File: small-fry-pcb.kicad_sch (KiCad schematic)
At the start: 139 parts, among them U1 Pico

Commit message: Squashed commit of the following:
commit e493926800ae8eeeb9c8551a418d401659cc4f4a
Author: anchovie-codes <littlebrother.free@gmail.com>
Date:   Sun Nov 10 19:39:24 2024 -0500

    updated edge cuts and gerbers

commit a852bf54e9e750d94bc40db8a16316f7cdac5ac1
Author: anchovie-codes <littlebrother.free@gmail.com>
Date:   Sat Sep 28 17:49:30 2024 -0400

    fixed rows, generated gerbers

commit 9d77bf2fb49dd0b8cbfb8cfda25d822d23244967
Author: anchovie-codes <littlebrother.free@gmail.com>
Date:   Sat Sep 28 13:01:13 2024 -0400

    fixed cols

commit 5f5487953ddbebd1258b34876b9f208a7da505d8
Author: anchovie-codes <littlebrother.free@gmail.com>
Date:   Fri Sep 27 21:14:36 2024 -0400

    made it a fish
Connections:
- net col0: now also U1.20 (GPIO15); no longer U1.19 (GPIO14)
- net col1: now also U1.19 (GPIO14); no longer U1.17 (GPIO13)
- net col10: now also U1.27 (GPIO21); no longer U1.6 (GPIO4)
- net col11: now also U1.26 (GPIO20); no longer U1.5 (GPIO3)
- net col12: now also U1.25 (GPIO19); no longer U1.4 (GPIO2)
- net col13: now also U1.24 (GPIO18); no longer U1.2 (GPIO1)
- net col14: now also U1.22 (GPIO17); no longer U1.1 (GPIO0)
- net col2: now also U1.17 (GPIO13); no longer U1.16 (GPIO12)
- net col3: now also U1.16 (GPIO12); no longer U1.15 (GPIO11)
- net col4: now also U1.15 (GPIO11); no longer U1.14 (GPIO10)
- net col5: now also U1.14 (GPIO10); no longer U1.12 (GPIO9)
- net col6: now also U1.12 (GPIO9); no longer U1.11 (GPIO8)
- net col7: now also U1.32 (GPIO27_ADC1); no longer U1.10 (GPIO7)
- net col8: now also U1.31 (GPIO26_ADC0); no longer U1.9 (GPIO6)
- net col9: now also U1.29 (GPIO22); no longer U1.7 (GPIO5)
- net row0: now also U1.6 (GPIO4); no longer U1.27 (GPIO21)
- net row1: now also U1.7 (GPIO5); no longer U1.26 (GPIO20)
- net row2: now also U1.9 (GPIO6); no longer U1.25 (GPIO19)
- net row3: now also U1.10 (GPIO7); no longer U1.24 (GPIO18)
- net row4: now also U1.11 (GPIO8); no longer U1.22 (GPIO17)
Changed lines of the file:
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@@
 	)
 	(no_connect
+		(at 20.32 29.21)
+	)
+	(no_connect
 		(at 55.88 69.85)
 	)
@@
 	)
 	(no_connect
-		(at 55.88 41.91)
+		(at 20.32 26.67)
 	)
 	(no_connect
@@
 	)
 	(no_connect
-		(at 55.88 54.61)
+		(at 55.88 41.91)
 	)
 	(no_connect
-		(at 55.88 49.53)
+		(at 40.64 80.01)
 	)
 	(no_connect
-		(at 40.64 80.01)
+		(at 20.32 34.29)
 	)
 	(no_connect
@@
 	)
 	(no_connect
-		(at 20.32 74.93)
-	)
-	(no_connect
-		(at 55.88 46.99)
+		(at 20.32 36.83)
 	)
 	(no_connect
@@
 		)
 	)
-	(global_label "col14"
-		(shape input)
-		(at 20.32 26.67 180)
-		(fields_autoplaced yes)
-		(effects
-			(font
-				(size 1.27 1.27)
-			)
-			(justify right)
-		)
-		(property "Intersheetrefs" "${INTERSHEET_REFS}"
-			(at 12.6672 26.67 0)
-			(effects
-				(font
-					(size 1.27 1.27)
-				)
-				(justify right)
-				(hide yes)
-			)
-		)
-	)
-	(global_label "row0"
+	(global_label "col10"
 		(shape input)
 		(at 55.88 59.69 0)
@@
 		)
 		(property "Intersheetrefs" "${INTERSHEET_REFS}"
-			(at 62.6862 59.69 0)
+			(at 63.5328 59.69 0)
 			(effects
 				(font
@@
 		)
 	)
-	(global_label "col13"
+	(global_label "col5"
 		(shape input)
-		(at 20.32 29.21 180)
+		(at 20.32 59.69 180)
 		(fields_autoplaced yes)
 		(effects
@@
 		)
 		(property "Intersheetrefs" "${INTERSHEET_REFS}"
-			(at 12.6672 29.21 0)
+			(at 13.8767 59.69 0)
 			(effects
 				(font
@@
 		)
 	)
-	(global_label "col12"
+	(global_label "col1"
 		(shape input)
-		(at 20.32 34.29 180)
+		(at 20.32 72.39 180)
 		(fields_autoplaced yes)
 		(effects
@@
 		)
 		(property "Intersheetrefs" "${INTERSHEET_REFS}"
-			(at 12.6672 34.29 0)
+			(at 13.8767 72.39 0)
 			(effects
 				(font
@@
 		)
 	)
-	(global_label "col4"
+	(global_label "col2"
 		(shape input)
-		(at 20.32 59.69 180)
-		(fields_autoplaced yes)
+		(at 102.616 24.892 90)
 		(effects
 			(font
 				(size 1.27 1.27)
 			)
-			(justify right)
+			(justify left)
 		)
 		(property "Intersheetrefs" "${INTERSHEET_REFS}"
-			(at 13.8767 59.69 0)
+			(at 102.616 24.892 0)
 			(effects
 				(font
 					(size 1.27 1.27)
 				)
-				(justify right)
 				(hide yes)
 			)
 		)
 	)
-	(global_label "col0"
+	(global_label "col4"
 		(shape input)
-		(at 20.32 72.39 180)
+		(at 20.32 62.23 180)
 		(fields_autoplaced yes)
 		(effects
@@
 		)
 		(property "Intersheetrefs" "${INTERSHEET_REFS}"
-			(at 13.8767 72.39 0)
+			(at 13.8767 62.23 0)
 			(effects
 				(font
@@
 		)
 	)
-	(global_label "col2"
+	(global_label "col14"
 		(shape input)
-		(at 102.616 24.892 90)
+		(at 55.88 72.39 0)
+		(fields_autoplaced yes)
 		(effects
 			(font
@@
 		)
 		(property "Intersheetrefs" "${INTERSHEET_REFS}"
-			(at 102.616 24.892 0)
+			(at 63.5328 72.39 0)
 			(effects
 				(font
 					(size 1.27 1.27)
 				)
+				(justify left)
 				(hide yes)
 			)
@@
 	(global_label "col3"
 		(shape input)
-		(at 20.32 62.23 180)
+		(at 20.32 64.77 180)
 		(fields_autoplaced yes)
 		(effects
@@
 		)
 		(property "Intersheetrefs" "${INTERSHEET_REFS}"
-			(at 13.8767 62.23 0)
+			(at 13.8767 64.77 0)
 			(effects
 				(font
@@
 		)
 	)
-	(global_label "row4"
+	(global_label "col7"
 		(shape input)
-		(at 55.88 72.39 0)
+		(at 55.88 46.99 0)
 		(fields_autoplaced yes)
 		(effects
@@
 		)
 		(property "Intersheetrefs" "${INTERSHEET_REFS}"
-			(at 62.6862 72.39 0)
+			(at 62.3233 46.99 0)
 			(effects
 				(font
@@
 		)
 	)
-	(global_label "col2"
-		(shape input)
-		(at 20.32 64.77 180)
-		(fields_autoplaced yes)
-		(effects
-			(font
-				(size 1.27 1.27)
-			)
-			(justify right)
-		)
-		(property "Intersheetrefs" "${INTERSHEET_REFS}"
-			(at 13.8767 64.77 0)
-			(effects
-				(font
-					(size 1.27 1.27)
-				)
-				(justify right)
-				(hide yes)
-			)
-		)
-	)
 	(global_label "row0"
 		(shape input)
@@
 		)
 	)
-	(global_label "row2"
+	(global_label "col12"
 		(shape input)
 		(at 55.88 64.77 0)
@@
 		)
 		(property "Intersheetrefs" "${INTERSHEET_REFS}"
-			(at 62.6862 64.77 0)
+			(at 63.5328 64.77 0)
 			(effects
 				(font
@@
 		)
 	)
-	(global_label "col9"
+	(global_label "row1"
 		(shape input)
 		(at 20.32 41.91 180)
@@
 		)
 		(property "Intersheetrefs" "${INTERSHEET_REFS}"
-			(at 13.8767 41.91 0)
+			(at 13.5138 41.91 0)
 			(effects
 				(font
@@
 		)
 	)
-	(global_label "row3"
+	(global_label "col13"
 		(shape input)
 		(at 55.88 67.31 0)
@@
 		)
 		(property "Intersheetrefs" "${INTERSHEET_REFS}"
-			(at 62.6862 67.31 0)
+			(at 63.5328 67.31 0)
 			(effects
 				(font
@@
 		)
 	)
+	(global_label "row4"
+		(shape input)
+		(at 20.32 52.07 180)
+		(fields_autoplaced yes)
+		(effects
+			(font
+				(size 1.27 1.27)
+			)
+			(justify right)
+		)
+		(property "Intersheetrefs" "${INTERSHEET_REFS}"
+			(at 13.5138 52.07 0)
+			(effects
+				(font
+					(size 1.27 1.27)
+				)
+				(justify right)
+				(hide yes)
+			)
+		)
+	)
 	(global_label "row1"
 		(shape input)
@@
 		)
 	)
-	(global_label "col11"
+	(global_label "col8"
 		(shape input)
-		(at 20.32 36.83 180)
+		(at 55.88 49.53 0)
 		(fields_autoplaced yes)
 		(effects
@@
 				(size 1.27 1.27)
 			)
-			(justify right)
+			(justify left)
 		)
 		(property "Intersheetrefs" "${INTERSHEET_REFS}"
-			(at 12.6672 36.83 0)
+			(at 62.3233 49.53 0)
 			(effects
 				(font
 					(size 1.27 1.27)
 				)
-				(justify right)
+				(justify left)
 				(hide yes)
 			)
 		)
 	)
-	(global_label "col7"
+	(global_label "row3"
 		(shape input)
 		(at 20.32 49.53 180)
@@
 		)
 		(property "Intersheetrefs" "${INTERSHEET_REFS}"
-			(at 13.8767 49.53 0)
+			(at 13.5138 49.53 0)
 			(effects
 				(font
@@
 		)
 	)
-	(global_label "col10"
+	(global_label "row0"
 		(shape input)
 		(at 20.32 39.37 180)
@@
 		)
 		(property "Intersheetrefs" "${INTERSHEET_REFS}"
-			(at 12.6672 39.37 0)
+			(at 13.5138 39.37 0)
 			(effects
 				(font
@@
 		)
 	)
-	(global_label "col6"
+	(global_label "col0"
 		(shape input)
-		(at 20.32 52.07 180)
+		(at 20.32 74.93 180)
 		(fields_autoplaced yes)
 		(effects
@@
 		)
 		(property "Intersheetrefs" "${INTERSHEET_REFS}"
-			(at 13.8767 52.07 0)
+			(at 13.8767 74.93 0)
 			(effects
 				(font
@@
 		)
 	)
-	(global_label "col8"
+	(global_label "row2"
 		(shape input)
 		(at 20.32 46.99 180)
@@
 		)
 		(property "Intersheetrefs" "${INTERSHEET_REFS}"
-			(at 13.8767 46.99 0)
+			(at 13.5138 46.99 0)
 			(effects
 				(font
@@
 		)
 	)
-	(global_label "row1"
+	(global_label "col11"
 		(shape input)
 		(at 55.88 62.23 0)
@@
 		)
 		(property "Intersheetrefs" "${INTERSHEET_REFS}"
-			(at 62.6862 62.23 0)
+			(at 63.5328 62.23 0)
 			(effects
 				(font
@@
 		)
 	)
-	(global_label "col1"
+	(global_label "col9"
+		(shape input)
+		(at 55.88 54.61 0)
+		(fields_autoplaced yes)
+		(effects
+			(font
+				(size 1.27 1.27)
+			)
+			(justify left)
+		)
+		(property "Intersheetrefs" "${INTERSHEET_REFS}"
+			(at 62.3233 54.61 0)
+			(effects
+				(font
+					(size 1.27 1.27)
+				)
+				(justify left)
+				(hide yes)
+			)
+		)
+	)
+	(global_label "col2"
 		(shape input)
 		(at 20.32 67.31 180)
@@
 		)
 	)
-	(global_label "col5"
+	(global_label "col6"
 		(shape input)
 		(at 20.32 54.61 180)

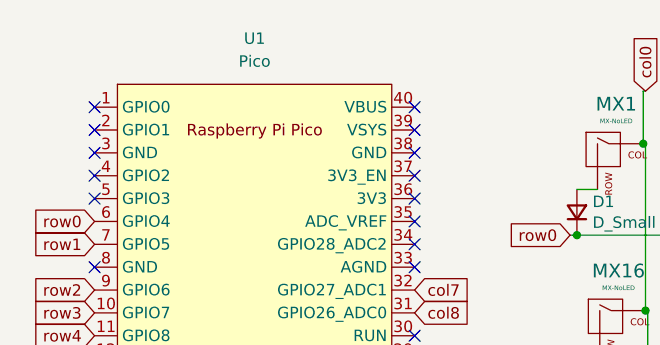
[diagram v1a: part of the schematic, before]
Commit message: updated and compiled firmware
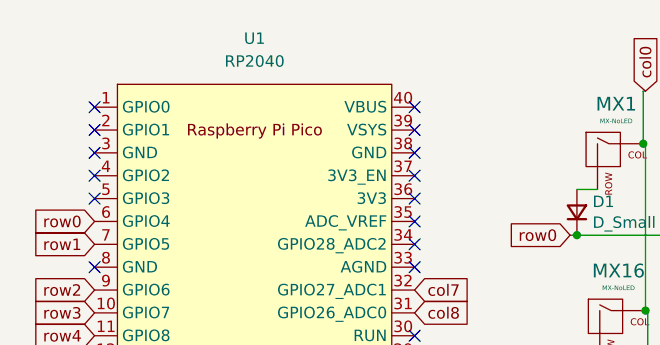
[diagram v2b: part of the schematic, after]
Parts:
- U1: value Pico -> RP2040
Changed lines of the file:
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@@
 			)
 		)
-		(property "Value" "Pico"
+		(property "Value" "RP2040"
 			(at 38.1 21.59 0)
 			(effects
